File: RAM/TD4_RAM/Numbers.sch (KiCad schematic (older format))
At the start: 0 parts

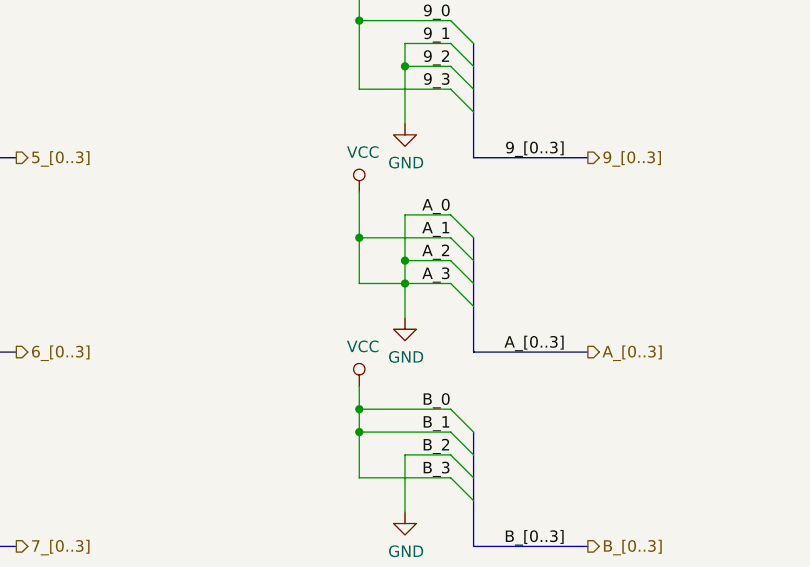
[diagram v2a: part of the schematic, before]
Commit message: Main RAM blocks routed
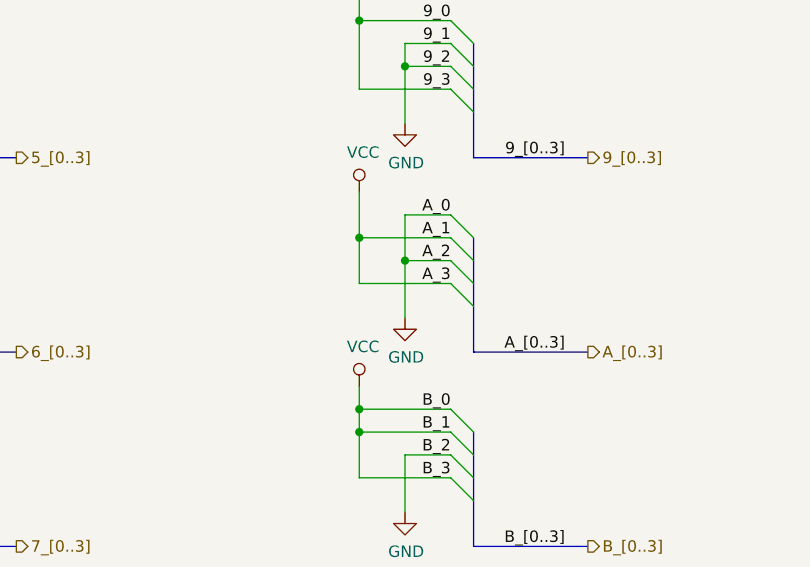
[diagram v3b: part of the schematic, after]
